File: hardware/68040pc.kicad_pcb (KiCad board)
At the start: 2 copper layers, 1 part

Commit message: add atx outline, begin DRAM schematic
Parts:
- added J1: ~, 68040:SIMM-72_23DEG, F.Cu at (332.3, 123.6)
- added J2: ~, 68040:SIMM-72_23DEG, F.Cu at (332.3, 138.4)
- added J3: ~, 68040:SIMM-72_23DEG, F.Cu at (332.3, 153.2)
- added J4: ~, 68040:SIMM-72_23DEG, F.Cu at (332.3, 167.9)
- added U2: ICE40HX4K-TQ144, Package_QFP:TQFP-144_20x20mm_P0.5mm, F.Cu at (311.9, 204.4)
- U1: value ~ -> 68LC040
- moved U1 195.5 mm to (233.7, 180.3)
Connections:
- U1 pad C7: (no net) -> unconnected-(U1-GND-PadC7)
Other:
- board outline added: 304.8 x 243.8 mm
- copper layers 2 -> 4

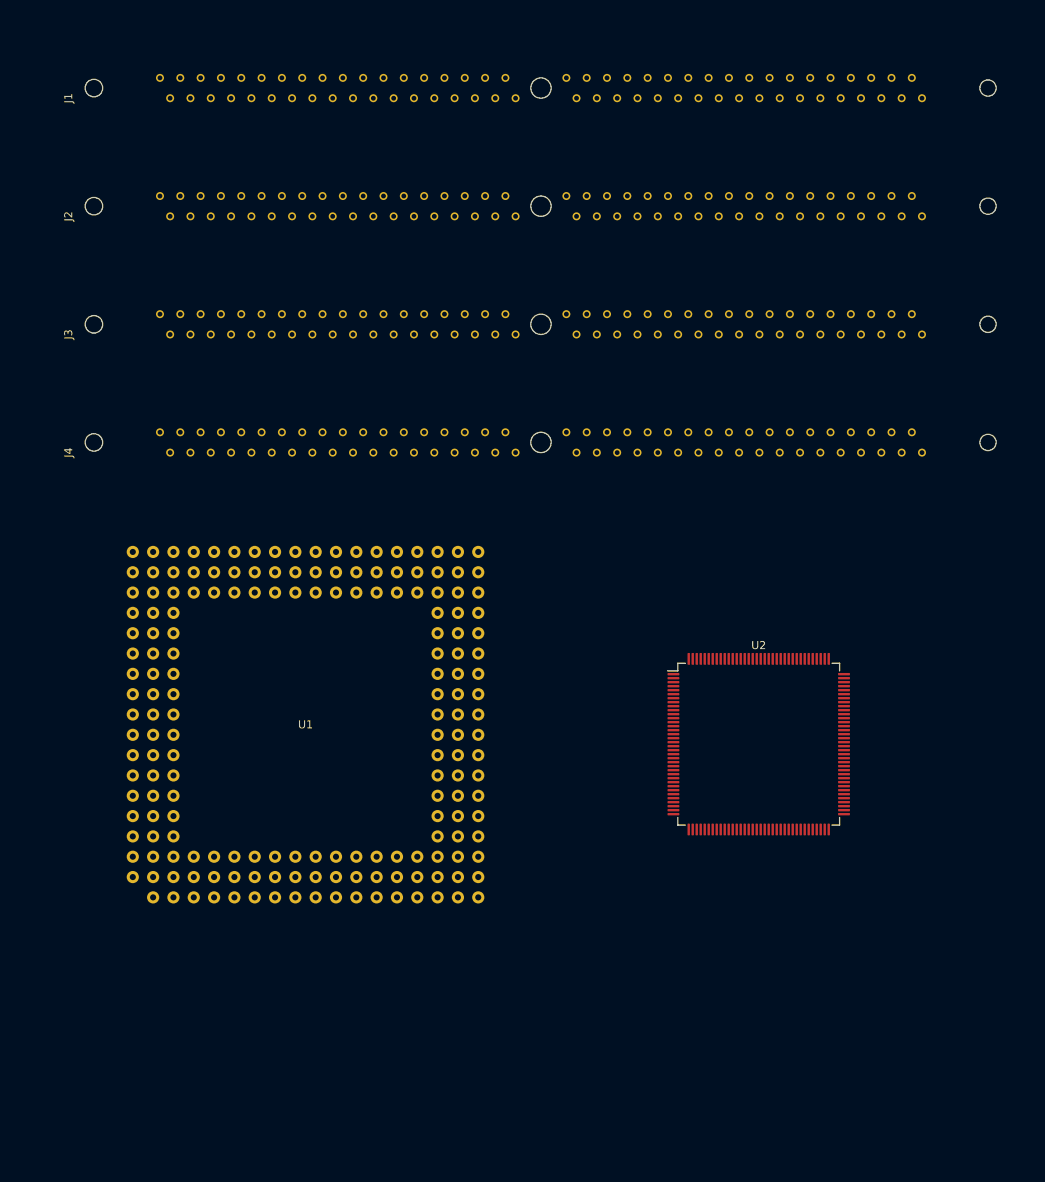
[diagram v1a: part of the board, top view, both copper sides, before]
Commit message: more memory wiring
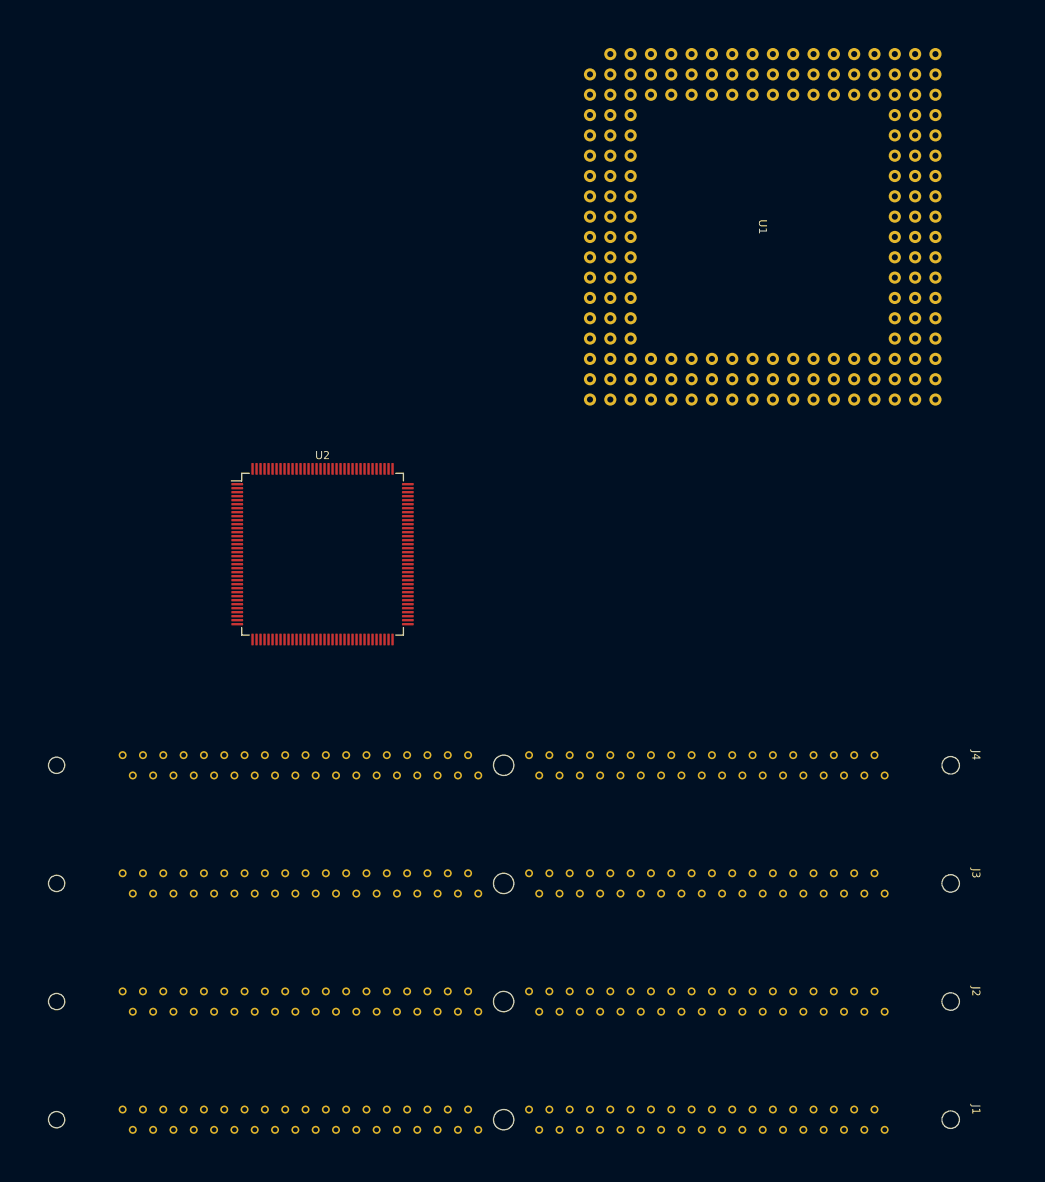
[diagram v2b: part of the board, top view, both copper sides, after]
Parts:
- moved J1 161.1 mm to (232.4, 250.0), turned to 180 degrees
- moved J2 139.2 mm to (232.4, 235.3), turned to 180 degrees
- moved J3 120.5 mm to (232.4, 220.5), turned to 180 degrees
- moved U1 118.1 mm to (334.0, 118.1), turned to -90 degrees
- moved J4 106.8 mm to (232.4, 205.7), turned to 180 degrees
- moved U2 59.5 mm to (257.4, 180.6)
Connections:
- U1 pad A1: unconnected-(U1-A31-PadA1) -> /Memory/A31
- U1 pad A10: unconnected-(U1-D12-PadA10) -> /Memory/D12
- U1 pad A11: unconnected-(U1-D13-PadA11) -> /Memory/D13
- U1 pad A12: unconnected-(U1-D14-PadA12) -> /Memory/D14
- U1 pad A13: unconnected-(U1-D15-PadA13) -> /Memory/D15
- U1 pad A14: unconnected-(U1-D17-PadA14) -> /Memory/D17
- U1 pad A15: unconnected-(U1-D19-PadA15) -> /Memory/D19
- U1 pad A16: unconnected-(U1-D20-PadA16) -> /Memory/D20
- U1 pad A17: unconnected-(U1-D21-PadA17) -> /Memory/D21
- U1 pad A18: unconnected-(U1-D24-PadA18) -> /Memory/D24
- U1 pad A2: unconnected-(U1-D3-PadA2) -> /Memory/D3
- U1 pad A3: unconnected-(U1-D4-PadA3) -> /Memory/D4
- U1 pad A4: unconnected-(U1-D5-PadA4) -> /Memory/D5
- U1 pad A5: unconnected-(U1-D6-PadA5) -> /Memory/D6
- U1 pad A6: unconnected-(U1-D7-PadA6) -> /Memory/D7
- U1 pad A7: unconnected-(U1-D9-PadA7) -> /Memory/D9
- U1 pad A8: unconnected-(U1-D10-PadA8) -> /Memory/D10
- U1 pad A9: unconnected-(U1-D11-PadA9) -> /Memory/D11
- U1 pad B1: unconnected-(U1-A29-PadB1) -> /Memory/A29
- U1 pad B11: unconnected-(U1-D16-PadB11) -> /Memory/D16
- U1 pad B12: unconnected-(U1-D18-PadB12) -> /Memory/D18
- U1 pad B16: unconnected-(U1-D22-PadB16) -> /Memory/D22
- U1 pad B18: unconnected-(U1-D26-PadB18) -> /Memory/D26
- U1 pad B3: unconnected-(U1-D1-PadB3) -> /Memory/D1
- U1 pad B7: unconnected-(U1-D8-PadB7) -> /Memory/D8
- U1 pad C1: unconnected-(U1-A27-PadC1) -> /Memory/A27
- U1 pad C15: unconnected-(U1-D23-PadC15) -> /Memory/D23
- U1 pad C16: unconnected-(U1-D25-PadC16) -> /Memory/D25
- U1 pad C18: unconnected-(U1-D28-PadC18) -> /Memory/D28
- U1 pad C3: unconnected-(U1-D0-PadC3) -> /Memory/D0
- U1 pad C4: unconnected-(U1-D2-PadC4) -> /Memory/D2
- U1 pad D1: unconnected-(U1-A24-PadD1) -> /Memory/A24
- U1 pad D16: unconnected-(U1-D27-PadD16) -> /Memory/D27
- U1 pad D18: unconnected-(U1-D31-PadD18) -> /Memory/D31
- U1 pad D3: unconnected-(U1-A30-PadD3) -> /Memory/A30
- U1 pad E1: unconnected-(U1-A22-PadE1) -> /Memory/A22
- U1 pad E16: unconnected-(U1-D29-PadE16) -> /Memory/D29
- U1 pad E17: unconnected-(U1-D30-PadE17) -> /Memory/D30
- U1 pad E18: unconnected-(U1-A8-PadE18) -> /Memory/A8
- U1 pad E2: unconnected-(U1-A26-PadE2) -> /Memory/A26
- U1 pad E3: unconnected-(U1-A28-PadE3) -> /Memory/A28
- U1 pad F1: unconnected-(U1-A21-PadF1) -> /Memory/A21
- U1 pad F16: unconnected-(U1-A9-PadF16) -> /Memory/A9
- U1 pad F18: unconnected-(U1-A7-PadF18) -> /Memory/A7
- U1 pad F3: unconnected-(U1-A25-PadF3) -> /Memory/A25
- U1 pad G1: unconnected-(U1-A20-PadG1) -> /Memory/A20
- U1 pad G16: unconnected-(U1-A6-PadG16) -> /Memory/A6
- U1 pad G18: unconnected-(U1-A5-PadG18) -> /Memory/A5
- U1 pad G3: unconnected-(U1-A23-PadG3) -> /Memory/A23
- U1 pad H1: unconnected-(U1-A18-PadH1) -> /Memory/A18
- U1 pad H18: unconnected-(U1-A4-PadH18) -> /Memory/A4
- U1 pad J1: unconnected-(U1-A17-PadJ1) -> /Memory/A17
- U1 pad J17: unconnected-(U1-A2-PadJ17) -> /Memory/A2
- U1 pad J18: unconnected-(U1-A3-PadJ18) -> /Memory/A3
- U1 pad J2: unconnected-(U1-A19-PadJ2) -> /Memory/A19
- U1 pad K1: unconnected-(U1-A15-PadK1) -> /Memory/A15
- U1 pad K18: unconnected-(U1-A1-PadK18) -> /Memory/A1
- U1 pad K2: unconnected-(U1-A16-PadK2) -> /Memory/A16
- U1 pad L1: unconnected-(U1-A14-PadL1) -> /Memory/A14
- U1 pad L18: unconnected-(U1-A0-PadL18) -> /Memory/A0
- U1 pad M1: unconnected-(U1-A13-PadM1) -> /Memory/A13
- U1 pad N1: unconnected-(U1-A12-PadN1) -> /Memory/A12
- U1 pad N3: unconnected-(U1-A11-PadN3) -> /Memory/A11
- U1 pad P1: unconnected-(U1-A10-PadP1) -> /Memory/A10
- U2 pad 101: unconnected-(U2B-IOR_160-Pad101) -> /Memory/A10
- U2 pad 102: unconnected-(U2B-IOR_161-Pad102) -> /Memory/A11
- U2 pad 104: unconnected-(U2B-IOR_164-Pad104) -> /Memory/A12
- U2 pad 105: unconnected-(U2B-IOR_165-Pad105) -> /Memory/A13
- U2 pad 106: unconnected-(U2B-IOR_166-Pad106) -> /Memory/A14
- U2 pad 107: unconnected-(U2B-IOR_167-Pad107) -> /Memory/A15
- U2 pad 110: unconnected-(U2A-IOT_168-Pad110) -> /Memory/A16
- U2 pad 112: unconnected-(U2A-IOT_169-Pad112) -> /Memory/A17
- U2 pad 113: unconnected-(U2A-IOT_170-Pad113) -> /Memory/A18
- U2 pad 114: unconnected-(U2A-IOT_171-Pad114) -> /Memory/A19
- U2 pad 115: unconnected-(U2A-IOT_172-Pad115) -> /Memory/A20
- U2 pad 116: unconnected-(U2A-IOT_173-Pad116) -> /Memory/A21
- U2 pad 117: unconnected-(U2A-IOT_174-Pad117) -> /Memory/A22
- U2 pad 118: unconnected-(U2A-IOT_177-Pad118) -> /Memory/A23
- U2 pad 119: unconnected-(U2A-IOT_178-Pad119) -> /Memory/A24
- U2 pad 120: unconnected-(U2A-IOT_179-Pad120) -> /Memory/A25
- U2 pad 121: unconnected-(U2A-IOT_181-Pad121) -> /Memory/A26
- U2 pad 122: unconnected-(U2A-IOT_190-Pad122) -> /Memory/A27
- U2 pad 124: unconnected-(U2A-IOT_191-Pad124) -> /Memory/A28
- U2 pad 125: unconnected-(U2A-IOT_192-Pad125) -> /Memory/A29
- U2 pad 128: unconnected-(U2A-IOT_197_GBIN1-Pad128) -> /Memory/A30
- U2 pad 129: unconnected-(U2A-IOT_198_GBIN0-Pad129) -> /Memory/A31
- U2 pad 37: unconnected-(U2C-IOB_56-Pad37) -> /Memory/DRAM_A0
- U2 pad 38: unconnected-(U2C-IOB_57-Pad38) -> /Memory/DRAM_A1
- U2 pad 39: unconnected-(U2C-IOB_61-Pad39) -> /Memory/DRAM_A2
- U2 pad 41: unconnected-(U2C-IOB_63-Pad41) -> /Memory/DRAM_A3
- U2 pad 42: unconnected-(U2C-IOB_64-Pad42) -> /Memory/DRAM_A4
- U2 pad 43: unconnected-(U2C-IOB_71-Pad43) -> /Memory/DRAM_A5
- U2 pad 44: unconnected-(U2C-IOB_72-Pad44) -> /Memory/DRAM_A6
- U2 pad 45: unconnected-(U2C-IOB_73-Pad45) -> /Memory/DRAM_A10
- U2 pad 47: unconnected-(U2C-IOB_79-Pad47) -> /Memory/DRAM_A7
- U2 pad 48: unconnected-(U2C-IOB_80-Pad48) -> /Memory/DRAM_A11
- U2 pad 49: unconnected-(U2C-IOB_81_GBIN5-Pad49) -> /Memory/DRAM_A8
- U2 pad 52: unconnected-(U2C-IOB_82_GBIN4-Pad52) -> /Memory/DRAM_A9
- U2 pad 55: unconnected-(U2C-IOB_91-Pad55) -> /Memory/~{RAS3}
- U2 pad 56: unconnected-(U2C-IOB_94-Pad56) -> /Memory/~{RAS2}
- U2 pad 60: unconnected-(U2C-IOB_95-Pad60) -> /Memory/~{RAS0}
- U2 pad 61: unconnected-(U2C-IOB_96-Pad61) -> /Memory/~{RAS1}
- U2 pad 88: unconnected-(U2B-IOR_137-Pad88) -> /Memory/A0
- U2 pad 90: unconnected-(U2B-IOR_138-Pad90) -> /Memory/A1
- U2 pad 91: unconnected-(U2B-IOR_139-Pad91) -> /Memory/A2
- U2 pad 93: unconnected-(U2B-IOR_140_GBIN3-Pad93) -> /Memory/A3
- U2 pad 94: unconnected-(U2B-IOR_141_GBIN2-Pad94) -> /Memory/A4
- U2 pad 95: unconnected-(U2B-IOR_144-Pad95) -> /Memory/A5
- U2 pad 96: unconnected-(U2B-IOR_146-Pad96) -> /Memory/A6
- U2 pad 97: unconnected-(U2B-IOR_147-Pad97) -> /Memory/A7
- U2 pad 98: unconnected-(U2B-IOR_148-Pad98) -> /Memory/A8
- U2 pad 99: unconnected-(U2B-IOR_152-Pad99) -> /Memory/A9

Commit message: lock position of expansion slots
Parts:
- added J10: EXP, 68040:EXP, F.Cu at (138.7, 114.8)
- added J11: EXP, 68040:EXP, F.Cu at (159.0, 114.8)
- added J12: EXP, 68040:EXP, F.Cu at (118.4, 114.8)
- added J13: EXP, 68040:EXP, F.Cu at (179.3, 114.8)
- added J14: EXP, 68040:EXP, F.Cu at (199.7, 114.8)
- added J15: EXP, 68040:EXP, F.Cu at (220.0, 114.8)
- added J5: DB25_Receptacle_MountingHoles, Connector_Dsub:DSUB-25_Male_Horizontal_P2.77x2.84mm_EdgePinOffset4.94mm_Housed_MountingHolesOffset7.48mm, F.Cu at (337.9, 76.2)
- added J6: DE9_Plug_MountingHoles, Connector_Dsub:DSUB-9_Male_Horizontal_P2.77x2.84mm_EdgePinOffset4.94mm_Housed_MountingHolesOffset7.48mm, F.Cu at (281.9, 76.2)
- added J7: DE9_Plug_MountingHoles, Connector_Dsub:DSUB-9_Male_Horizontal_P2.77x2.84mm_EdgePinOffset4.94mm_Housed_MountingHolesOffset7.48mm, F.Cu at (248.9, 76.2)
- added J8: EXP, 68040:EXP, F.Cu at (77.7, 114.8)
- added J9: EXP, 68040:EXP, F.Cu at (98.1, 114.8)
- J1, J2, J3, J4: footprint 68040:SIMM-72_23DEG -> 68040:SIMM-72
- moved J4 127.2 mm to (340.4, 273.1), turned to 0 degrees
- moved J3 115.5 mm to (340.4, 261.6), turned to 0 degrees
- moved J2 109.0 mm to (340.4, 250.2), turned to 0 degrees
- moved J1 108.5 mm to (340.4, 238.8), turned to 0 degrees
- moved U1 4.02 mm to (332.7, 121.9)
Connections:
- U1 pad B10: unconnected-(U1-GND-PadB10) -> /GND_{O}
- U1 pad B13: unconnected-(U1-GND-PadB13) -> /GND_{O}
- U1 pad B14: unconnected-(U1-V_{CC}-PadB14) -> /V_{CC}_{O}
- U1 pad B15: unconnected-(U1-GND-PadB15) -> /GND_{O}
- U1 pad B17: unconnected-(U1-GND-PadB17) -> /GND_{O}
- U1 pad B2: unconnected-(U1-GND-PadB2) -> /GND_{O}
- U1 pad B4: unconnected-(U1-GND-PadB4) -> /GND_{O}
- U1 pad B5: unconnected-(U1-V_{CC}-PadB5) -> /V_{CC}_{O}
- U1 pad B6: unconnected-(U1-GND-PadB6) -> /GND_{O}
- U1 pad B8: unconnected-(U1-GND-PadB8) -> /GND_{O}
- U1 pad B9: unconnected-(U1-V_{CC}-PadB9) -> /V_{CC}_{O}
- U1 pad C10: unconnected-(U1-V_{CC}-PadC10) -> /V_{CC}_{L}
- U1 pad C11: unconnected-(U1-GND-PadC11) -> /GND_{L}
- U1 pad C12: unconnected-(U1-V_{CC}-PadC12) -> /V_{CC}_{L}
- U1 pad C13: unconnected-(U1-GND-PadC13) -> /GND_{L}
- U1 pad C14: unconnected-(U1-V_{CC}-PadC14) -> /V_{CC}_{L}
- U1 pad C17: unconnected-(U1-V_{CC}-PadC17) -> /V_{CC}_{O}
- U1 pad C2: unconnected-(U1-V_{CC}-PadC2) -> /V_{CC}_{O}
- U1 pad C5: unconnected-(U1-V_{CC}-PadC5) -> /V_{CC}_{L}
- U1 pad C6: unconnected-(U1-GND-PadC6) -> /GND_{L}
- U1 pad C7: unconnected-(U1-GND-PadC7) -> /GND_{L}
- U1 pad C8: unconnected-(U1-V_{CC}-PadC8) -> /V_{CC}_{L}
- U1 pad C9: unconnected-(U1-GND-PadC9) -> /GND_{L}
- U1 pad D17: unconnected-(U1-GND-PadD17) -> /GND_{O}
- U1 pad D2: unconnected-(U1-GND-PadD2) -> /GND_{O}
- U1 pad F17: unconnected-(U1-GND-PadF17) -> /GND_{O}
- U1 pad F2: unconnected-(U1-GND-PadF2) -> /GND_{O}
- U1 pad G17: unconnected-(U1-V_{CC}-PadG17) -> /V_{CC}_{O}
- U1 pad G2: unconnected-(U1-V_{CC}-PadG2) -> /V_{CC}_{O}
- U1 pad H16: unconnected-(U1-V_{CC}-PadH16) -> /V_{CC}_{L}
- U1 pad H17: unconnected-(U1-GND-PadH17) -> /GND_{O}
- U1 pad H2: unconnected-(U1-GND-PadH2) -> /GND_{O}
- U1 pad H3: unconnected-(U1-V_{CC}-PadH3) -> /V_{CC}_{L}
- U1 pad J16: unconnected-(U1-V_{CC}-PadJ16) -> /V_{CC}_{L}
- U1 pad J3: unconnected-(U1-V_{CC}-PadJ3) -> /V_{CC}_{L}
- U1 pad K16: unconnected-(U1-GND-PadK16) -> /GND_{L}
- U1 pad K17: unconnected-(U1-TM2-PadK17) -> /TM2
- U1 pad K3: unconnected-(U1-GND-PadK3) -> /GND_{L}
- U1 pad L16: unconnected-(U1-V_{CC}-PadL16) -> /V_{CC}_{L}
- U1 pad L17: unconnected-(U1-GND-PadL17) -> /GND_{O}
- U1 pad L2: unconnected-(U1-GND-PadL2) -> /GND_{O}
- U1 pad L3: unconnected-(U1-GND-PadL3) -> /GND_{L}
- U1 pad M16: unconnected-(U1-GND-PadM16) -> /GND_{L}
- U1 pad M17: unconnected-(U1-V_{CC}-PadM17) -> /V_{CC}_{O}
- U1 pad M18: unconnected-(U1-TM1-PadM18) -> /TM1
- U1 pad M2: unconnected-(U1-V_{CC}-PadM2) -> /V_{CC}_{O}
- U1 pad M3: unconnected-(U1-V_{CC}-PadM3) -> /V_{CC}_{L}
- U1 pad N16: unconnected-(U1-R/~{W}-PadN16) -> /R/~{W}
- U1 pad N17: unconnected-(U1-GND-PadN17) -> /GND_{O}
- U1 pad N18: unconnected-(U1-TM0-PadN18) -> /TM0
- U1 pad N2: unconnected-(U1-GND-PadN2) -> /GND_{O}
- U1 pad P16: unconnected-(U1-SIZ1-PadP16) -> /SIZ1
- U1 pad P17: unconnected-(U1-SIZ0-PadP17) -> /SIZ0
- U1 pad P18: unconnected-(U1-TLN1-PadP18) -> /TLN1
- U1 pad P2: unconnected-(U1-TT1-PadP2) -> /TT1
- U1 pad P3: unconnected-(U1-TT0-PadP3) -> /TT0
- U1 pad Q1: unconnected-(U1-UPA1-PadQ1) -> /UPA1
- U1 pad Q16: unconnected-(U1-~{MI}-PadQ16) -> /~{MI}
- U1 pad Q17: unconnected-(U1-GND-PadQ17) -> /GND_{O}
- U1 pad Q18: unconnected-(U1-TLN0-PadQ18) -> /TLN0
- U1 pad Q2: unconnected-(U1-GND-PadQ2) -> /GND_{O}
- U1 pad Q3: unconnected-(U1-UPA0-PadQ3) -> /UPA0
- U1 pad R1: unconnected-(U1-~{CIOUT}-PadR1) -> /~{CIOUT}
- U1 pad R10: unconnected-(U1-GND-PadR10) -> /GND_{P}
- U1 pad R11: unconnected-(U1-GND-PadR11) -> /GND_{L}
- U1 pad R12: unconnected-(U1-V_{CC}-PadR12) -> /V_{CC}_{L}
- U1 pad R13: unconnected-(U1-GND-PadR13) -> /GND_{L}
- U1 pad R14: unconnected-(U1-PST2-PadR14) -> /PST2
- U1 pad R15: unconnected-(U1-~{TIP}-PadR15) -> /~{TIP}
- U1 pad R16: unconnected-(U1-~{TS}-PadR16) -> /~{TS}
- U1 pad R17: unconnected-(U1-V_{CC}-PadR17) -> /V_{CC}_{O}
- U1 pad R18: unconnected-(U1-~{LOCKE}-PadR18) -> /~{LOCKE}
- U1 pad R2: unconnected-(U1-V_{CC}-PadR2) -> /V_{CC}_{O}
- U1 pad R3: unconnected-(U1-~{RSTO}-PadR3) -> /~{RSTO}
- U1 pad R4: unconnected-(U1-GND-PadR4) -> /GND_{L}
- U1 pad R5: unconnected-(U1-V_{CC}-PadR5) -> /V_{CC}_{L}
- U1 pad R6: unconnected-(U1-GND-PadR6) -> /GND_{P}
- U1 pad R7: unconnected-(U1-BCLK-PadR7) -> /BCLK
- U1 pad R8: unconnected-(U1-V_{CC}-PadR8) -> /V_{CC}_{P}
- U1 pad R9: unconnected-(U1-PCLK-PadR9) -> /PCLK
- U1 pad S1: unconnected-(U1-~{IPEND}-PadS1) -> /~{IPEND}
- U1 pad S10: unconnected-(U1-GND-PadS10) -> /GND_{L}
- U1 pad S11: unconnected-(U1-~{TBI}-PadS11) -> /~{TBI}
- U1 pad S12: unconnected-(U1-SC1-PadS12) -> /SC1
- U1 pad S13: unconnected-(U1-~{TEA}-PadS13) -> /~{TEA}
- U1 pad S14: unconnected-(U1-PST1-PadS14) -> /PST1
- U1 pad S15: unconnected-(U1-GND-PadS15) -> /GND_{O}
- U1 pad S16: unconnected-(U1-V_{CC}-PadS16) -> /V_{CC}_{O}
- U1 pad S17: unconnected-(U1-GND-PadS17) -> /GND_{O}
- U1 pad S18: unconnected-(U1-~{LOCK}-PadS18) -> /~{LOCK}
- U1 pad S2: unconnected-(U1-GND-PadS2) -> /GND_{O}
- U1 pad S3: unconnected-(U1-TDI-PadS3) -> /TDI
- U1 pad S4: unconnected-(U1-TCK-PadS4) -> /TCK
- U1 pad S5: unconnected-(U1-TMS-PadS5) -> /TMS
- U1 pad S6: unconnected-(U1-~{MDIS}-PadS6) -> /~{MDIS}
- U1 pad S7: unconnected-(U1-~{RSTI}-PadS7) -> /~{RSTI}
- U1 pad S8: unconnected-(U1-V_{CC}-PadS8) -> /V_{CC}_{P}
- U1 pad S9: unconnected-(U1-GND-PadS9) -> /GND_{P}
- U1 pad T10: unconnected-(U1-~{TCI}-PadT10) -> /~{TCI}
- U1 pad T11: unconnected-(U1-~{AVEC}-PadT11) -> /~{AVEC}
- U1 pad T12: unconnected-(U1-SC0-PadT12) -> /SC0
- U1 pad T13: unconnected-(U1-~{BG}-PadT13) -> /~{BG}
- U1 pad T14: unconnected-(U1-~{TA}-PadT14) -> /~{TA}
- U1 pad T15: unconnected-(U1-PST0-PadT15) -> /PST0
- U1 pad T16: unconnected-(U1-PST3-PadT16) -> /PST3
- U1 pad T17: unconnected-(U1-~{BB}-PadT17) -> /~{BB}
- U1 pad T18: unconnected-(U1-~{BR}-PadT18) -> /~{BR}
- U1 pad T2: unconnected-(U1-TDO-PadT2) -> /TDO
- U1 pad T3: unconnected-(U1-~{TRST}-PadT3) -> /~{TSRT}
- U1 pad T4: unconnected-(U1-GND-PadT4) -> /GND_{L}
- U1 pad T5: unconnected-(U1-~{CDIS}-PadT5) -> /~{CDIS}
- U1 pad T6: unconnected-(U1-~{IPL2}-PadT6) -> /~{IPL2}
- U1 pad T7: unconnected-(U1-~{IPL1}-PadT7) -> /~{IPL1}
- U1 pad T8: unconnected-(U1-~{IPL0}-PadT8) -> /~{IPL0}
- U1 pad T9: unconnected-(U1-JS0-PadT9) -> /JS0

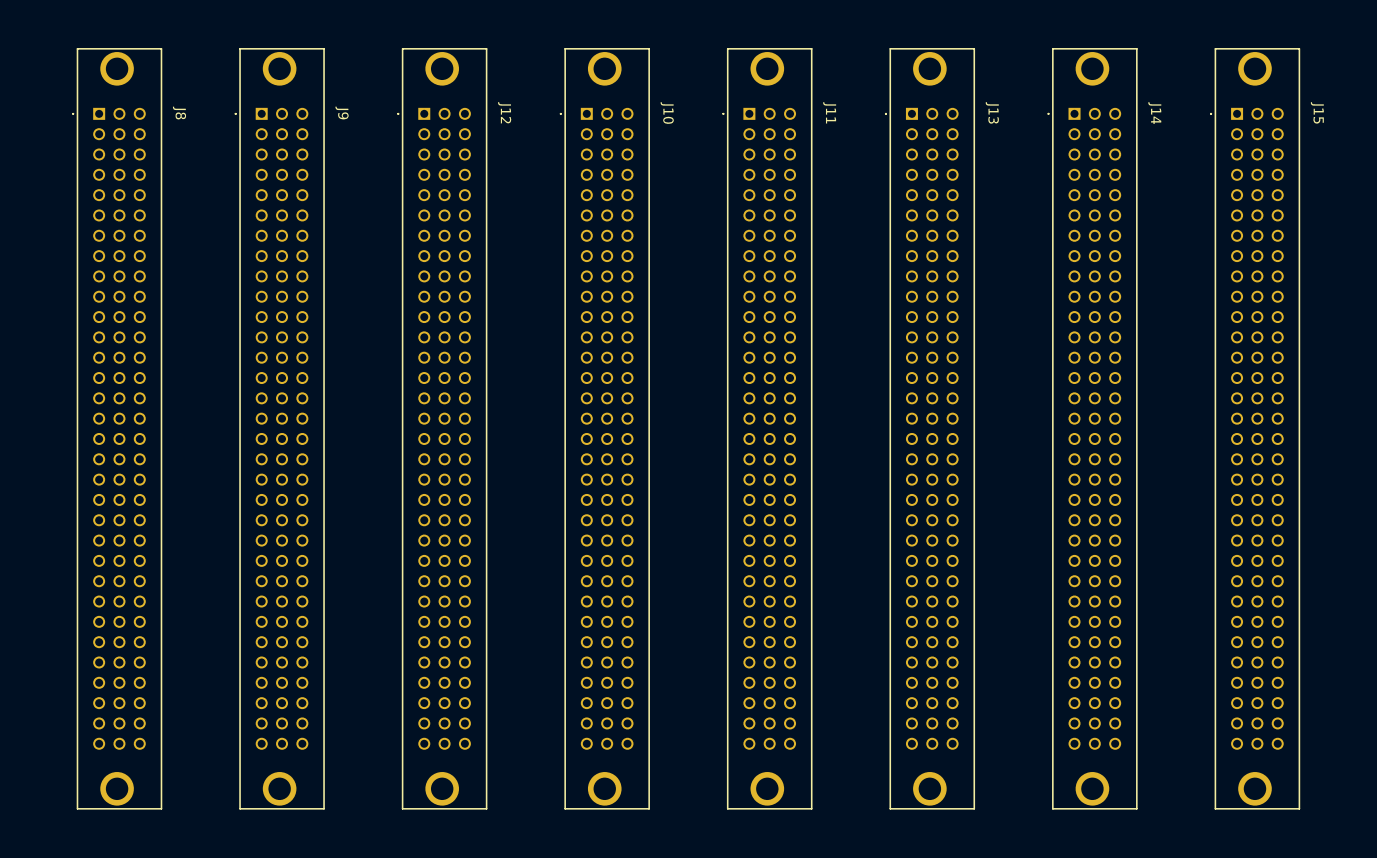
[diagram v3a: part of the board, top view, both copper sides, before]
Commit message: fix slot orientation (slot 1 only)\nTodo.. fix other slots
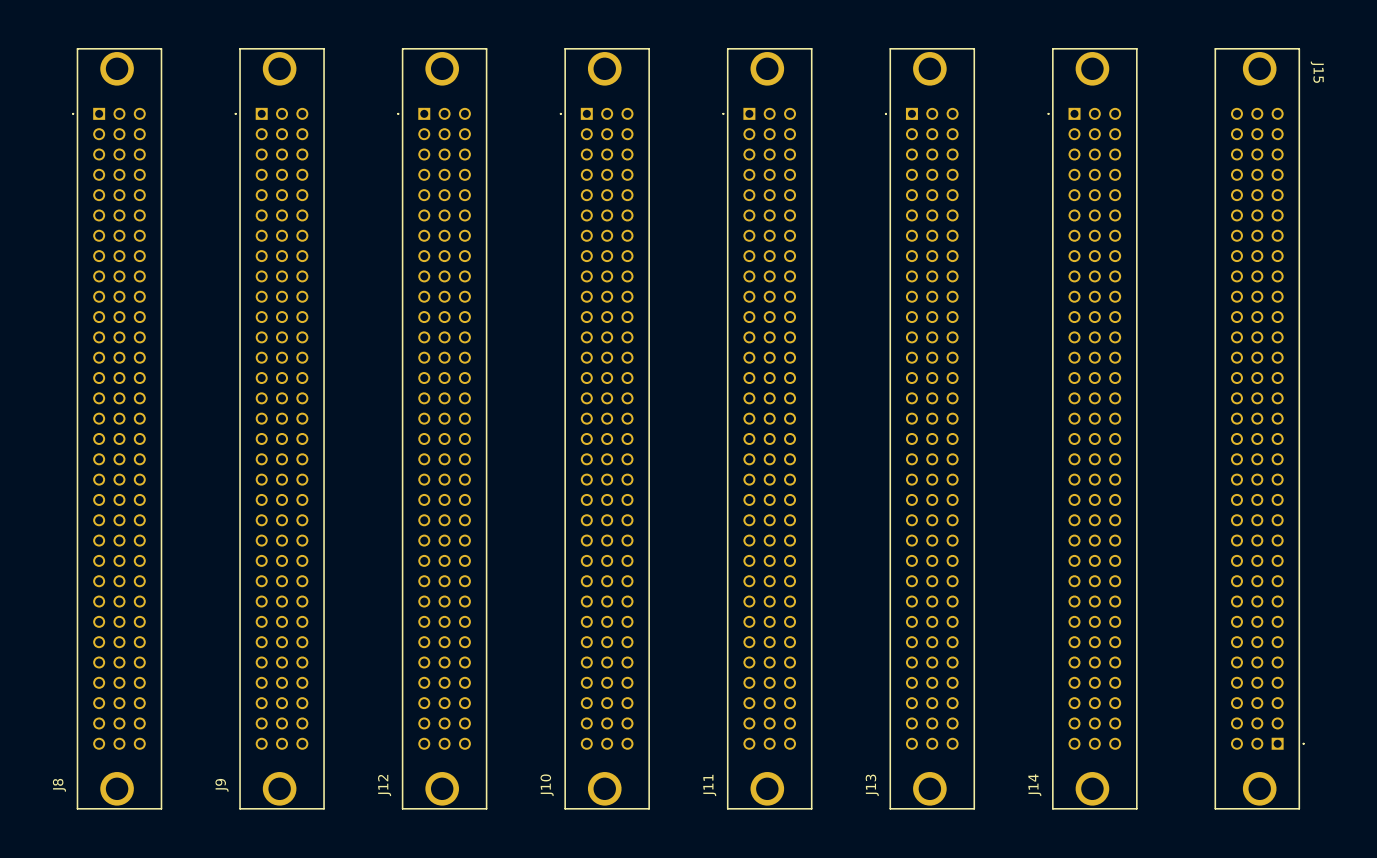
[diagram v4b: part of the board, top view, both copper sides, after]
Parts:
- moved J15 78.9 mm to (225.0, 193.5), turned to -90 degrees
